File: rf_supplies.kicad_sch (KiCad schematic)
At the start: 29 parts, among them J2 VSENSE, U1 INA290A2xDCK, U2 INA290A2xDCK

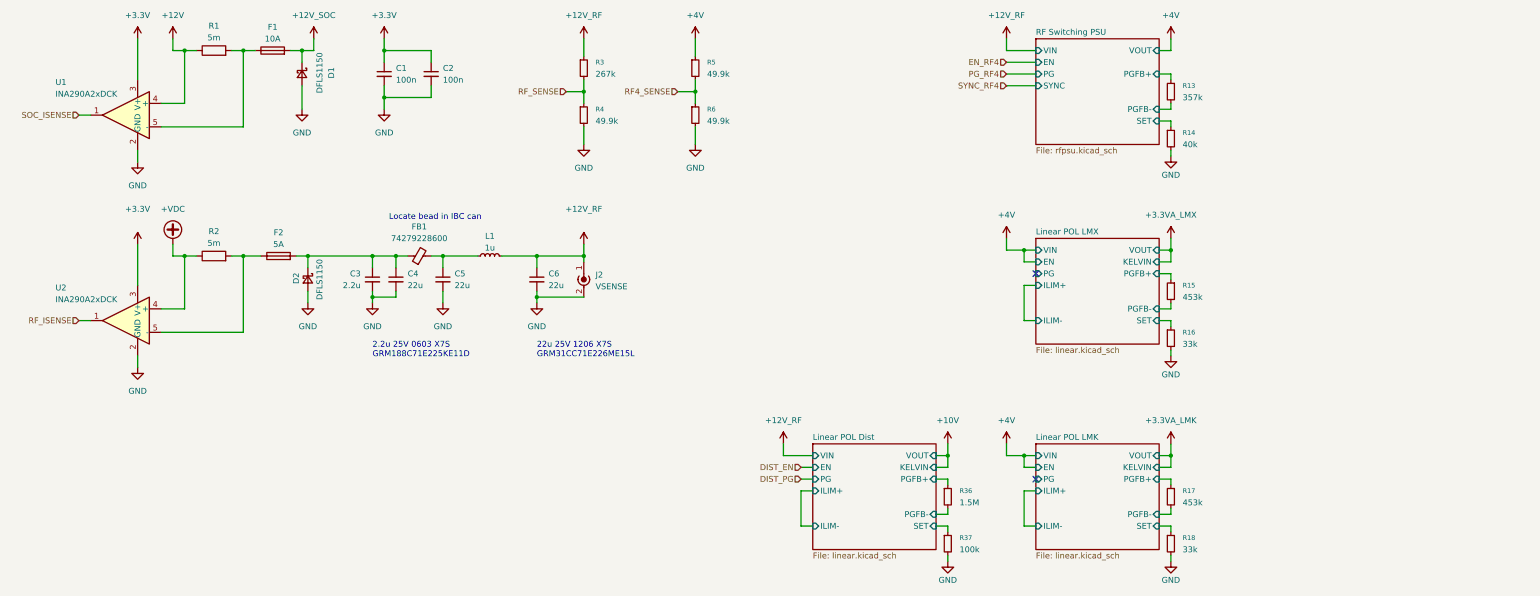
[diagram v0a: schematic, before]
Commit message: Renumber refdes
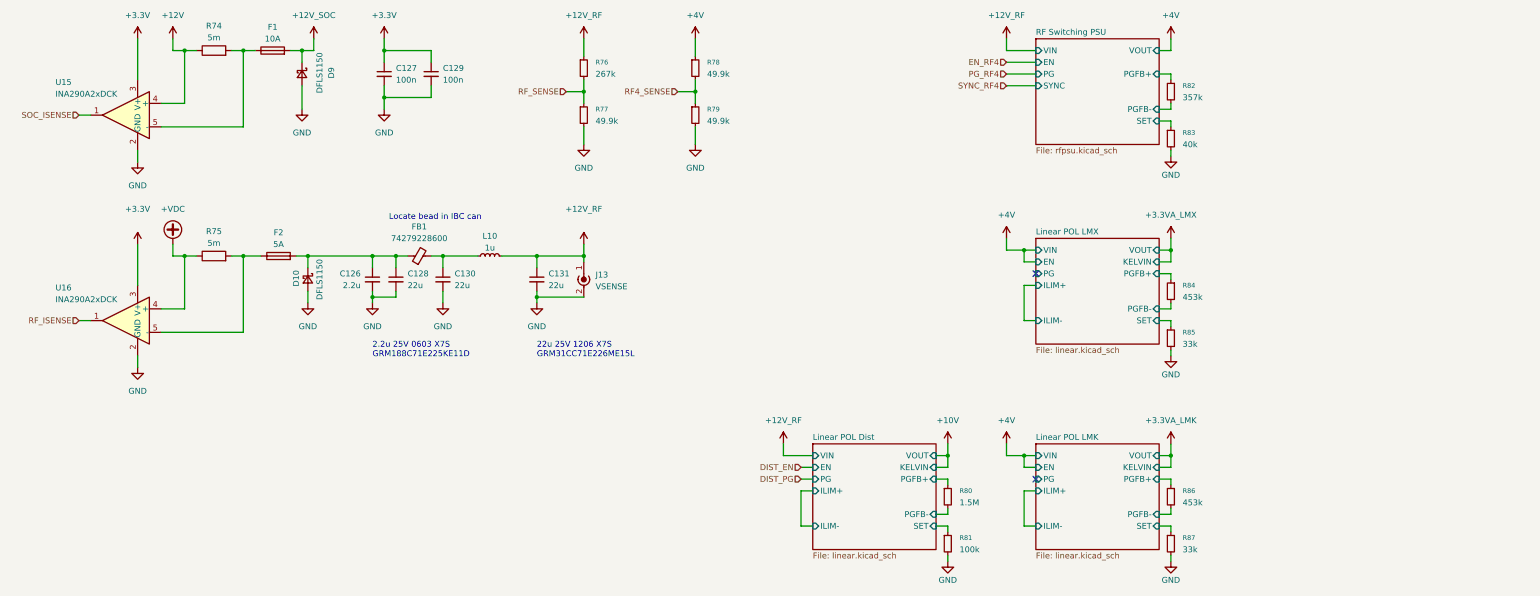
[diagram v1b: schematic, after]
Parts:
- renumbered C3 to C126, C1 to C127, C4 to C128, C2 to C129, C5 to C130, C6 to C131, D2 to D10, D1 to D9, J2 to J13, L1 to L10, R1 to R74, R2 to R75, R3 to R76, R4 to R77, R5 to R78, R6 to R79, R36 to R80, R37 to R81, R13 to R82, R14 to R83, R15 to R84, R16 to R85, R17 to R86, R18 to R87, U1 to U15, U2 to U16

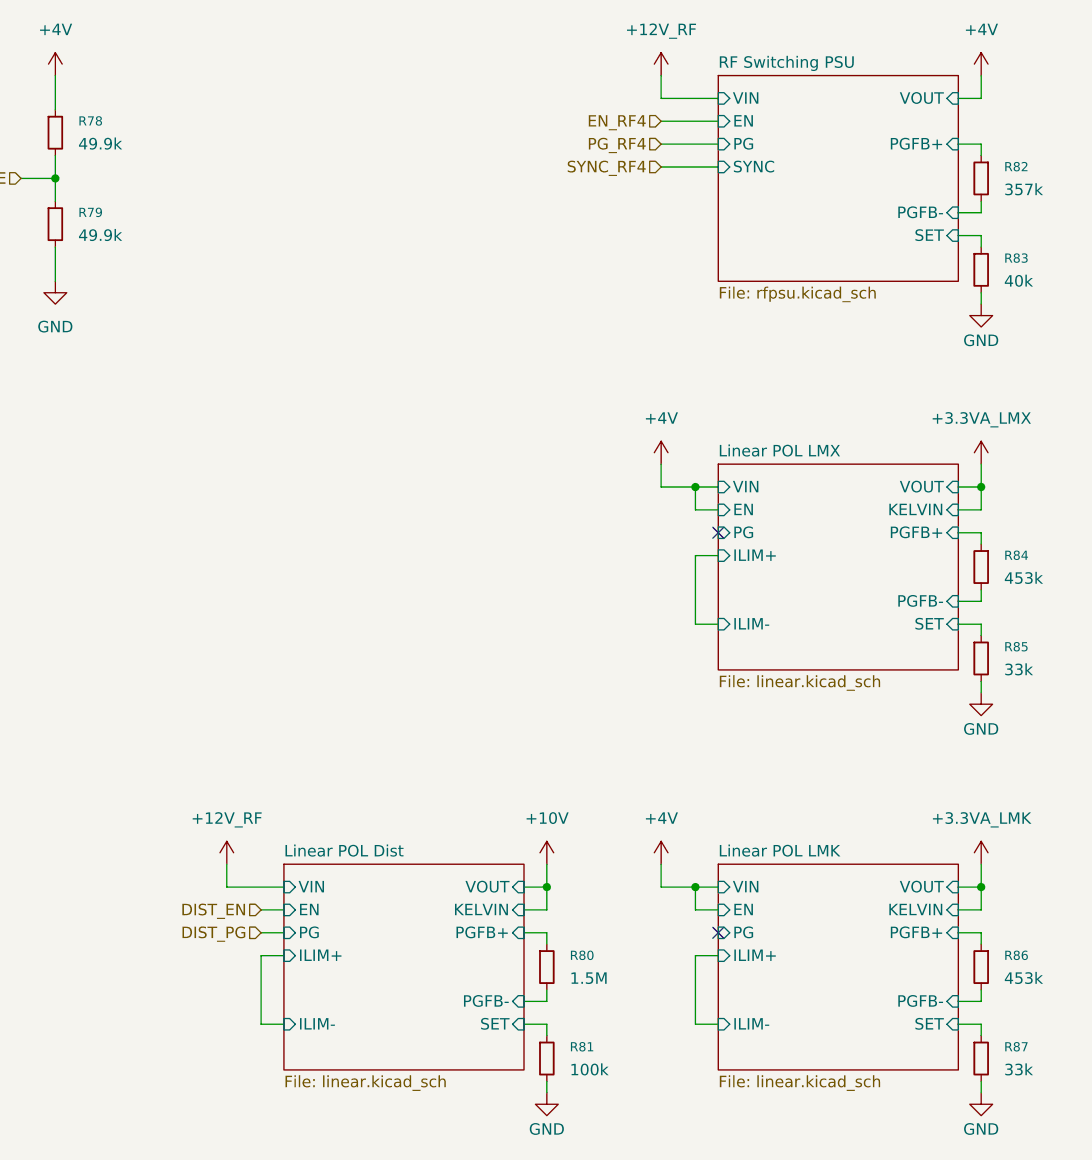
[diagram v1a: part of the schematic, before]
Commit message: Add lmk and bump schematic size
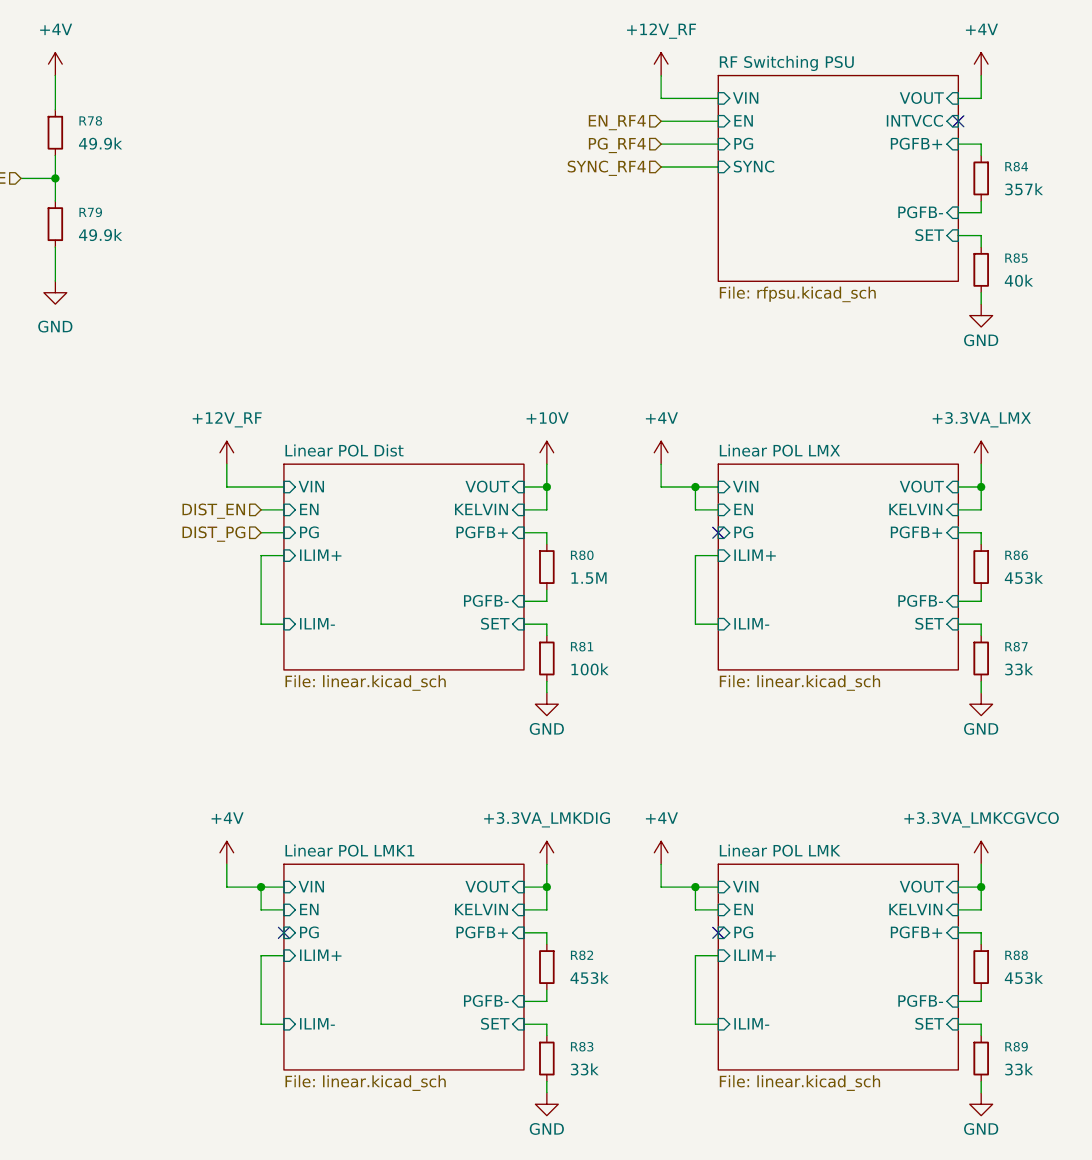
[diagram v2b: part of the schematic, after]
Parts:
- added R82: 453k, Resistor_SMD:R_0402_1005Metric, symbol Device:R_Small
- added R83: 33k, Resistor_SMD:R_0402_1005Metric, symbol Device:R_Small
- renumbered R82 to R84, R83 to R85, R84 to R86, R85 to R87, R86 to R88, R87 to R89
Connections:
- net GND: now also R83.2
- new net Linear POL LMK1/PGFB+: R82.1
- new net Linear POL LMK1/PGFB-: R82.2
- new net Linear POL LMK1/SET: R83.1
- no-connect marks 2 -> 4
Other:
- added sheet Linear POL LMK1 (linear.kicad_sch)
- sheet RF Switching PSU ports: added INTVCC; removed none
- moved on the sheet: R80, R81

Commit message: Add LMX Draft
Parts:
- added R92, R94: 453k, Resistor_SMD:R_0402_1005Metric, symbol Device:R_Small
- added R93, R95: 33k, Resistor_SMD:R_0402_1005Metric, symbol Device:R_Small
- renumbered R74 to R76, R75 to R77, R76 to R78, R77 to R79, R78 to R80, R79 to R81, R84 to R82, R85 to R83, R80 to R84, R81 to R85, R82 to R86, R83 to R87, R86 to R88, R87 to R89, R88 to R90, R89 to R91
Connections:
- net GND: now also R93.2, R95.2
- new net Linear POL LMX BUF/PGFB+: R92.1
- new net Linear POL LMX BUF/PGFB-: R92.2
- new net Linear POL LMX BUF/SET: R93.1
- new net Linear POL LMX PLL/PGFB+: R94.1
- new net Linear POL LMX PLL/PGFB-: R94.2
- new net Linear POL LMX PLL/SET: R95.1
- no-connect marks 4 -> 6
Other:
- sheet Linear POL LMK renamed Linear POL LMK VCO
- sheet Linear POL LMK1 renamed Linear POL LMK DIG
- sheet Linear POL LMX renamed Linear POL LMX DIG
- added sheet Linear POL LMX BUF (linear.kicad_sch)
- added sheet Linear POL LMX PLL (linear.kicad_sch)
- moved on the sheet: R82, R83, R84, R85, R86, R87, R88, R89, R90, R91

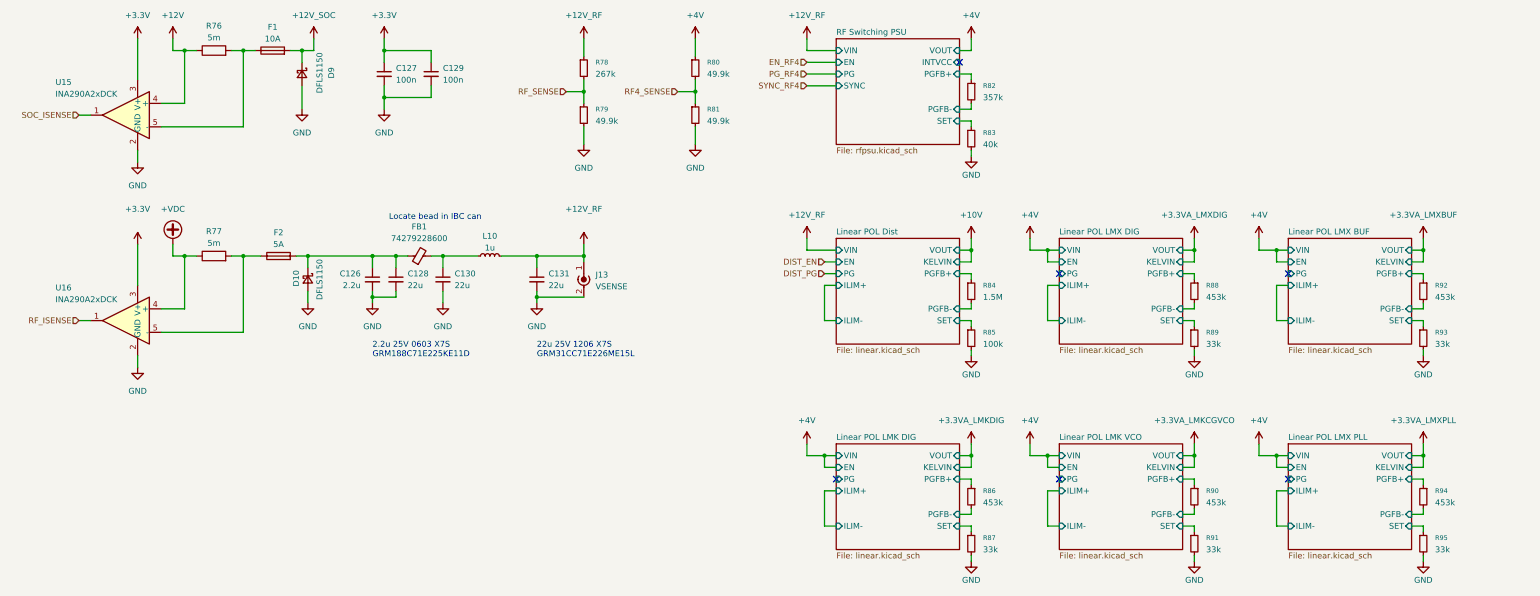
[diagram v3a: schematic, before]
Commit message: Different Matching Circuit
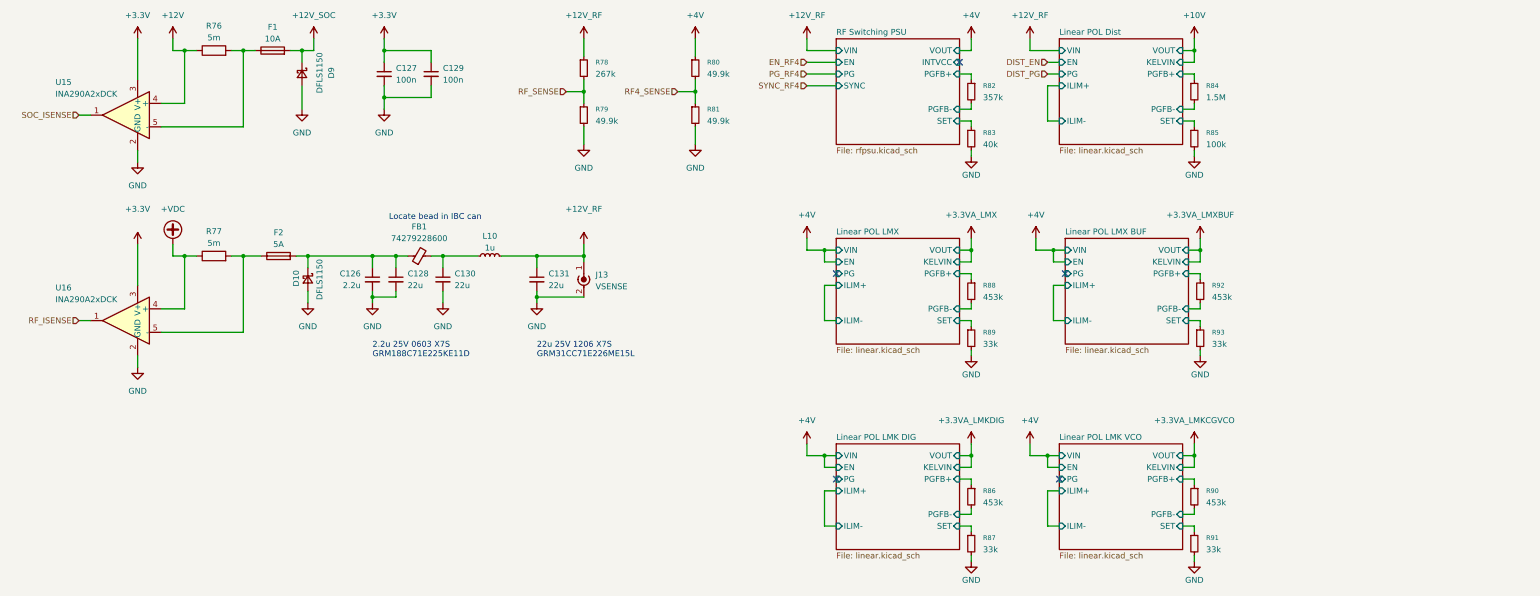
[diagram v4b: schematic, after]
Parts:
- removed R94: 453k, Resistor_SMD:R_0402_1005Metric, symbol Device:R_Small
- removed R95: 33k, Resistor_SMD:R_0402_1005Metric, symbol Device:R_Small
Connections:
- no-connect marks 6 -> 5
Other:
- sheet Linear POL LMX DIG renamed Linear POL LMX
- removed sheet Linear POL LMX PLL
- moved on the sheet: R84, R85, R88, R89, R92, R93

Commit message: Add mixer
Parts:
- added R244: 357k, Resistor_SMD:R_0402_1005Metric, symbol Device:R_Small
- added R245: 60k, Resistor_SMD:R_0402_1005Metric, symbol Device:R_Small
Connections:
- net GND: now also R245.2
- new net Switching TX 6V/PGFB+: R244.1
- new net Switching TX 6V/PGFB-: R244.2
- new net Switching TX 6V/SET: R245.1
- no-connect marks 5 -> 6
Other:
- added sheet Switching TX 6V (rfpsu.kicad_sch)
- moved on the sheet: R84, R85, R90, R91, R92, R93

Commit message: WIP Splitrail
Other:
- added sheet OP Amp Supply (splitrail.kicad_sch)
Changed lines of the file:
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@@
+	)
+	(sheet
+		(at 309.88 68.58)
+		(size 26.67 22.86)
+		(exclude_from_sim no)
+		(in_bom yes)
+		(on_board yes)
+		(dnp no)
+		(fields_autoplaced yes)
+		(stroke
+			(width 0.1524)
+			(type solid)
+		)
+		(fill
+			(color 0 0 0 0.0000)
+		)
+		(property "Sheetname" "OP Amp Supply"
+			(at 309.88 67.8684 0)
+			(effects
+				(font
+					(size 1.27 1.27)
+				)
+				(justify left bottom)
+			)
+		)
+		(property "Sheetfile" "splitrail.kicad_sch"
+			(at 309.88 92.0246 0)
+			(effects
+				(font
+					(size 1.27 1.27)
+				)
+				(justify left top)
+			)
+		)
+		(instances
+			(project "huskypointofload"
+				(path "/eb9c972b-d134-41da-be97-ece3f463f7e0/28dccbc8-62a2-4750-b12f-4e220cef19bd"
+					(page "21")
+				)
+			)
+		)
 	)
 	(sheet

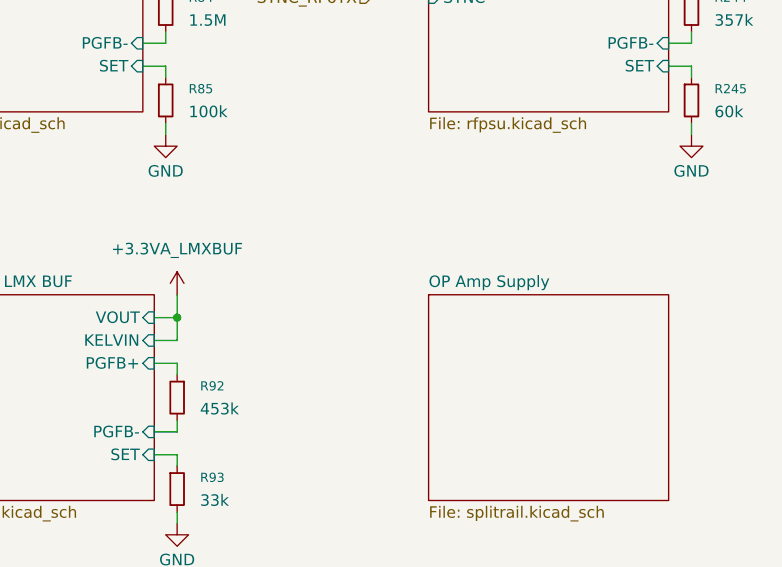
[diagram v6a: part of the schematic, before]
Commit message: Add VVA Bias generator
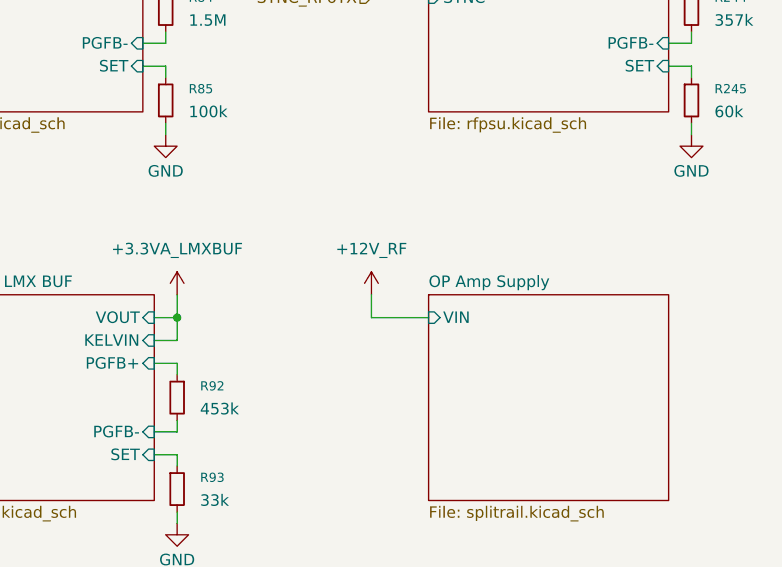
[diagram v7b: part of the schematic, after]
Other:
- sheet OP Amp Supply ports: added VIN; removed none
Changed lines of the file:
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@@
 	(wire
 		(pts
+			(xy 303.53 71.12) (xy 309.88 71.12)
+		)
+		(stroke
+			(width 0)
+			(type default)
+		)
+	)
+	(wire
+		(pts
 			(xy 251.46 123.19) (xy 248.92 123.19)
 		)
@@
 	(wire
 		(pts
+			(xy 303.53 68.58) (xy 303.53 71.12)
+		)
+		(stroke
+			(width 0)
+			(type default)
+		)
+	)
+	(wire
+		(pts
 			(xy 190.5 30.48) (xy 196.85 30.48)
 		)
@@
 	)
 	(symbol
+		(lib_id "power:+12V")
+		(at 303.53 68.58 0)
+		(unit 1)
+		(exclude_from_sim no)
+		(in_bom yes)
+		(on_board yes)
+		(dnp no)
+		(fields_autoplaced yes)
+		(property "Reference" "#PWR0151"
+			(at 303.53 72.39 0)
+			(effects
+				(font
+					(size 1.27 1.27)
+				)
+				(hide yes)
+			)
+		)
+		(property "Value" "+12V_RF"
+			(at 303.53 63.5 0)
+			(effects
+				(font
+					(size 1.27 1.27)
+				)
+			)
+		)
+		(property "Footprint" ""
+			(at 303.53 68.58 0)
+			(effects
+				(font
+					(size 1.27 1.27)
+				)
+				(hide yes)
+			)
+		)
+		(property "Datasheet" ""
+			(at 303.53 68.58 0)
+			(effects
+				(font
+					(size 1.27 1.27)
+				)
+				(hide yes)
+			)
+		)
+		(property "Description" "Power symbol creates a global label with name \"+12V\""
+			(at 303.53 68.58 0)
+			(effects
+				(font
+					(size 1.27 1.27)
+				)
+				(hide yes)
+			)
+		)
+		(pin "1"
+		)
+		(instances
+			(project "huskypointofload"
+				(path "/eb9c972b-d134-41da-be97-ece3f463f7e0/28dccbc8-62a2-4750-b12f-4e220cef19bd"
+					(reference "#PWR0151")
+					(unit 1)
+				)
+			)
+		)
+	)
+	(symbol
 		(lib_id "power:VBUS")
 		(at 142.24 69.85 0)
@@
 			)
 		)
+		(pin "VIN" input
+			(at 309.88 71.12 180)
+			(effects
+				(font
+					(size 1.27 1.27)
+				)
+				(justify left)
+			)
+		)
